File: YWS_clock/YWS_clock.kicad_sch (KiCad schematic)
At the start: 59 parts, among them J1 Conn_01x06, J2 PJ-102AH, J3 Conn_01x06, SW1 Omron_B3F_SPST, SW2 Omron_B3F_SPST, SW3 Omron_B3F_SPST, SW4 Omron_B3F_SPST, U1 L7805, U2 ATmega328-PU, U3 DS1307_DIP-8, U4 MAX7219, U5 MAX7219, U6 MAX7219, U7 MAX7219, Y1 Crystal_16MHz, Y2 Crystal_16MHz

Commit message: Add ICSP and separate sections
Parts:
- removed J2: PJ-102AH, footprints:PJ-102AH, symbol HPS:PJ-102AH
- removed R14: R_0805_10K, footprints:R_0805_2012Metric, symbol HPS:R_0805_10K
- removed R15: PhotoconductivePhotocell, footprints:R_LDR_4.9x4.2mm_P2.54mm_Vertical, symbol HPS:PhotoconductivePhotocell
- removed R5, R6: R_0805_2.2K, footprints:R_0805_2012Metric, symbol HPS:R_0805_2.2K
- added J2: Power_inlet_vertical, footprints:Wurth-694106402002, symbol HPS:Power_inlet_vertical
- added J4: Conn_01x06, footprints:PinHeader_2x03_P2.54mm_Vertical, symbol HPS:Conn_01x06
- added R14: PhotoconductivePhotocell, footprints:R_LDR_4.9x4.2mm_P2.54mm_Vertical, symbol HPS:PhotoconductivePhotocell
- added R15: R_0805_100K, footprints:R_0805_2012Metric, symbol HPS:R_0805_100K
- added R5, R6: R_0805_4.7K, footprints:R_0805_2012Metric, symbol HPS:R_0805_4.7K
- U1: footprint footprints:TO-220-3_Horizontal_TabDown -> footprints:TO-252-2
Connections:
- net GND: now also SW2.3 (B), SW2.4 (B), SW3.3 (B), SW3.4 (B), SW4.3 (B), SW4.4 (B), J2.2 (OUT), J4.6 (Pin_6), R15.2; no longer R11.2, R12.2, R13.2
- net LED_SCK: now also U2.19 (PB5), J4.3 (Pin_3); no longer U2.15 (PB1), U2.18 (PB4)
- net RESET: now also J4.5 (Pin_5)
- net RXD: now also U2.2 (PD0); no longer U2.12 (PD6)
- net TXD: now also U2.3 (PD1); no longer U2.13 (PD7)
- net VCC: now also R11.1, R12.1, R13.1, J4.2 (Pin_2), R14.1, R5.1, R6.1; no longer SW2.1 (A), SW2.2 (A), SW3.1 (A), SW3.2 (A), SW4.1 (A), SW4.2 (A)
- net at C6.1, U1.1 (IN): now also J2.1 (POLE)
- net BTN_SEL: now reaches U2.4 (PD2)
- net BTN_SEL: now also R11.2, SW2.1 (A), SW2.2 (A)
- net DISP_LOAD: now reaches U4.12 (LOAD), U5.12 (LOAD), U6.12 (LOAD), U7.12 (LOAD)
- net DISP_LOAD: now also U2.14 (PB0); no longer U2.16 (PB2)
- net DISP_CLK: now reaches U4.13 (CLK), U5.13 (CLK), U6.13 (CLK), U7.13 (CLK)
- net DISP_CLK: now also U2.15 (PB1); no longer U2.19 (PB5)
- net BTN_DOWN: now reaches U2.6 (PD4)
- net BTN_DOWN: now also R13.2, SW4.1 (A), SW4.2 (A)
- net SDA: now reaches U2.27 (PC4)
- net SDA: now also U3.5 (SDA), R6.2; no longer SW4.3 (B)
- net JOYST_X: now reaches J3.4 (Pin_4)
- net JOYST_X: now also U2.11 (PD5); no longer U2.23 (PC0)
- net BUZZER: now reaches U2.24 (PC1)
- net BUZZER: now also BZ1.2 (+); no longer J3.5 (Pin_5)
- net JOYST_Z: now reaches J3.6 (Pin_6)
- net JOYST_Z: now also U2.13 (PD7); no longer U2.11 (PD5)
- net SCL: now reaches U3.6 (SCL)
- net SCL: now also U2.28 (PC5), R5.2; no longer U2.2 (PD0)
- net DISP_DATA: now reaches U4.1 (DIN)
- net DISP_DATA: now also U2.16 (PB2); no longer U2.17 (PB3)
- net at U2.25 (PC2): no longer SW2.3 (B)
- net at U2.26 (PC3): no longer SW3.3 (B)
- net BTN_UP: now reaches U2.5 (PD3)
- net BTN_UP: now also R12.2, SW3.1 (A), SW3.2 (A); no longer BZ1.2 (+)
- new net JOYST_Y: J3.5 (Pin_5), U2.12 (PD6)
- new net LIGHT_SENSOR: R14.2, R15.1, U2.23 (PC0)
- new net MDSI: J4.4 (Pin_4)
- new net MISD: J4.1 (Pin_1)
- new net MISO: U2.18 (PB4)
- new net MOSI: U2.17 (PB3)
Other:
- note added: "Button"
- note added: "Buzzer"
- note added: "Dot Matrix with MAX7219"
- note added: "ICSP"
- note added: "JoyStick"
- note added: "Light Sensor"
- note added: "Mechanical"
- moved on the sheet: BT1, C1, C10, C11, C12, C13, C14, C15, C2, C3, C4, C5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

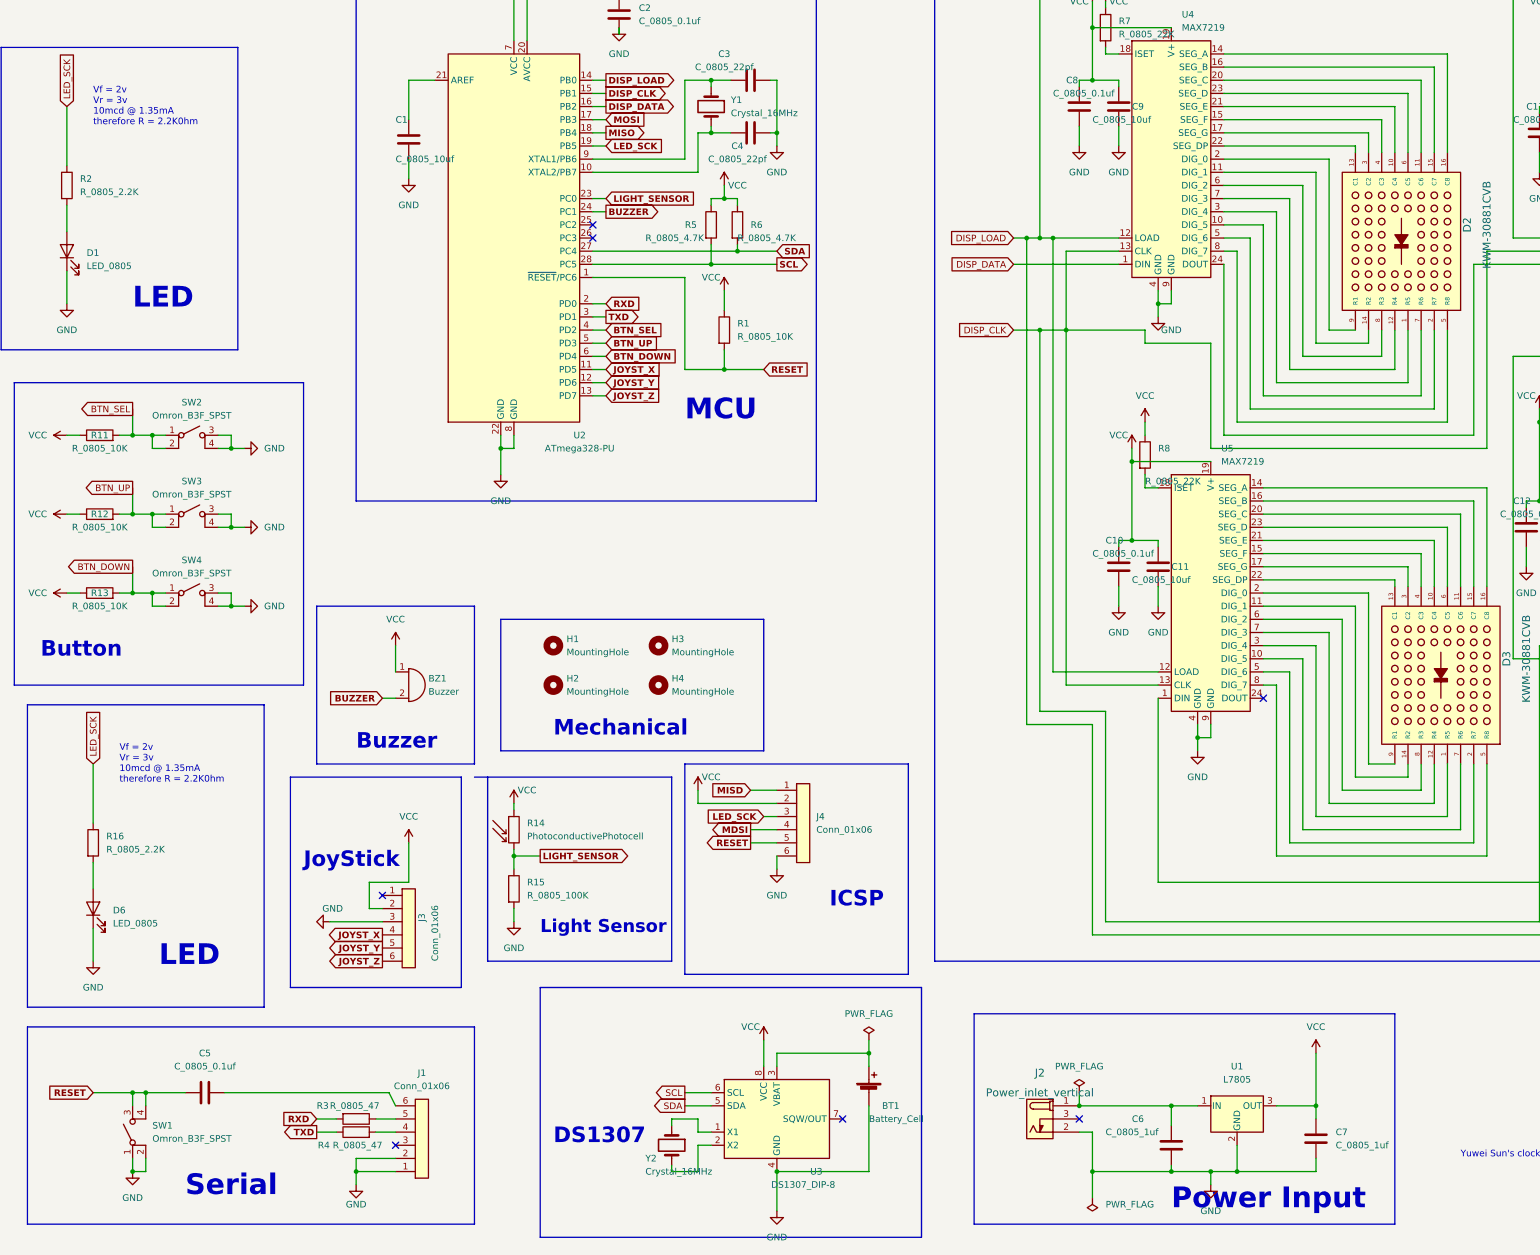
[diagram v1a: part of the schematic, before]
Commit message: Initial version with full routing and test point
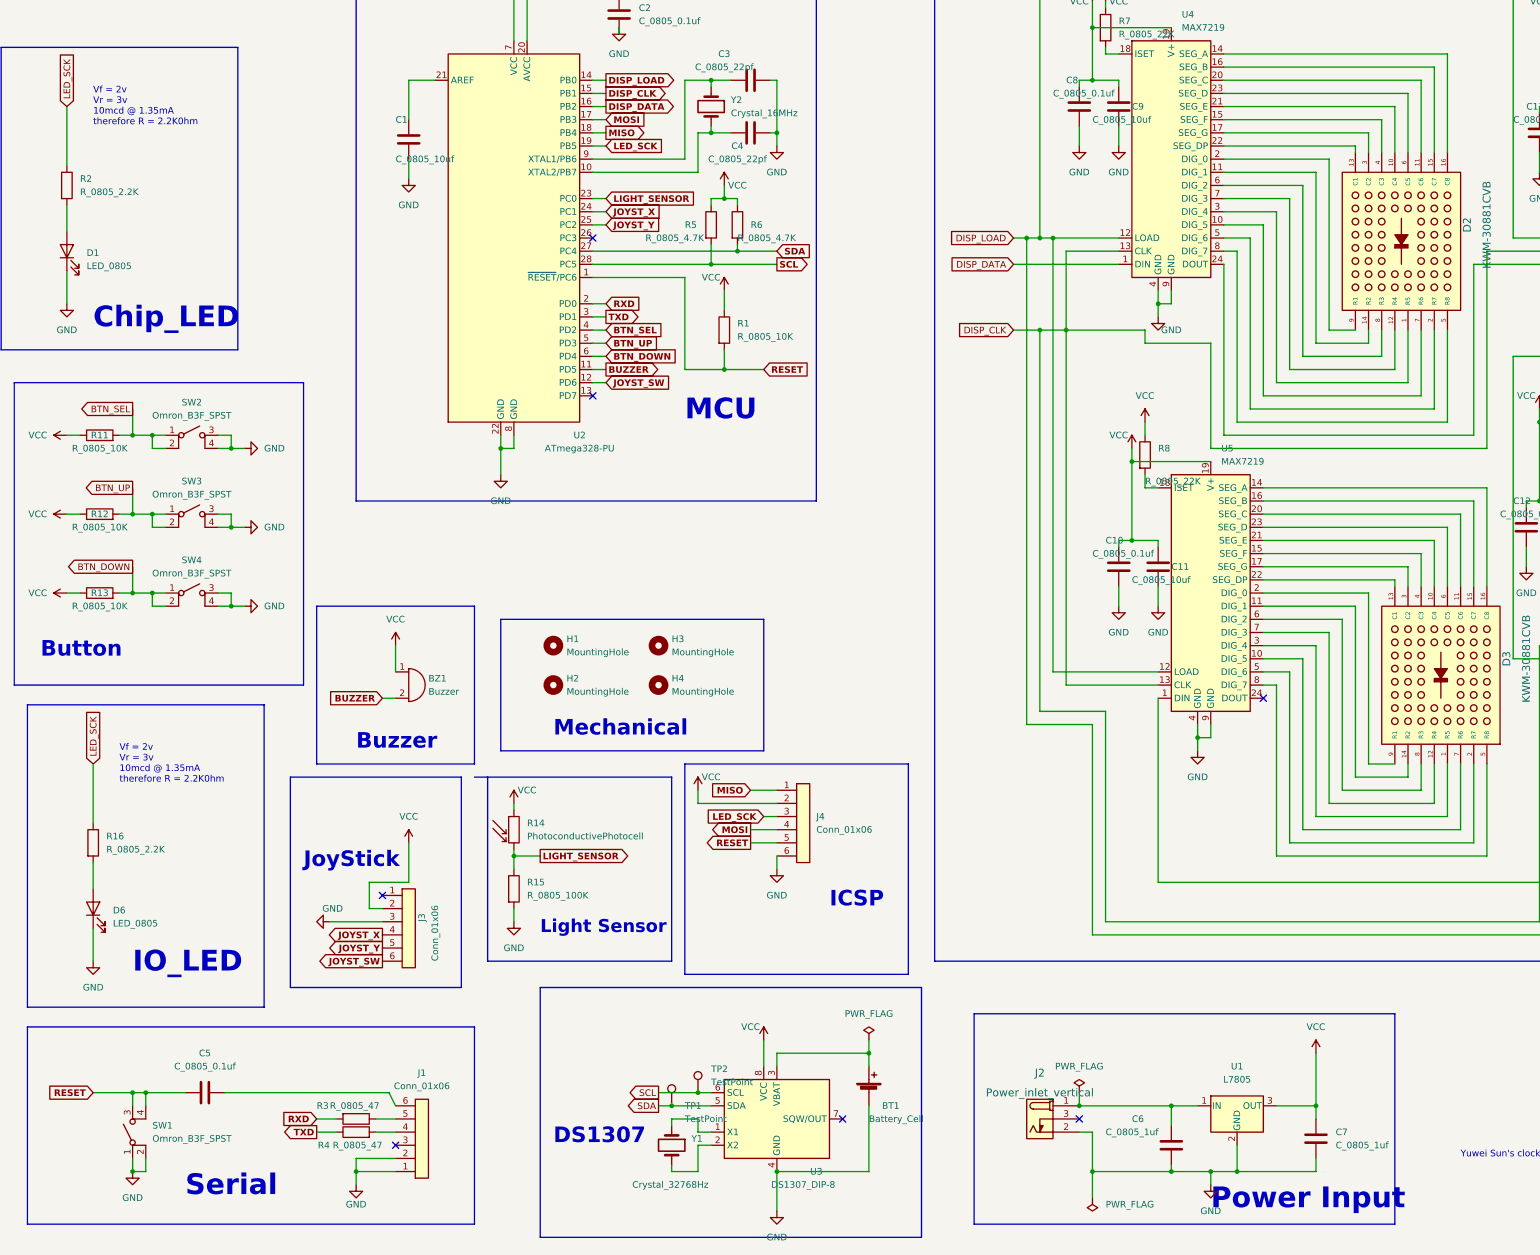
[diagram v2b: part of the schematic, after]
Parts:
- removed Y1: Crystal_16MHz, footprints:Crystal_SMD_HC49-SD, symbol HPS:Crystal_16MHz
- added TP1, TP2: TestPoint, footprints:TestPoint_THTPad_D2.0mm_Drill1.0mm, symbol HPS:TestPoint
- added Y1: Crystal_32768Hz, footprints:Crystal_SMD_2Pin_3.2x1.5mm, symbol HPS:Crystal_32768Hz
- U1: Digikey PN (none) -> 497-7255-1-ND; MFG (none) -> STMicroelectronics; MPN (none) -> L7805CDT-TR
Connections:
- net MDSI is gone; now on net MOSI: J4.4 (Pin_4)
- net MISD is gone; now on net MISO: J4.1 (Pin_1)
- net BUZZER: now also U2.11 (PD5); no longer U2.24 (PC1)
- net JOYST_X: now also U2.24 (PC1); no longer U2.11 (PD5)
- net JOYST_Y: now also U2.25 (PC2); no longer U2.12 (PD6)
- net SCL: now also TP2.1
- net SDA: now also TP1.1
- net at C3.1, U2.9 (XTAL1/PB6): now also Y2.1
- net at C4.1, U2.10 (XTAL2/PB7): now also Y2.2
- net at U3.1 (X1): now also Y1.1; no longer Y2.1
- net at U3.2 (X2): now also Y1.2; no longer Y2.2
- net JOYST_Z: no longer names the net of U2.13 (PD7)
- net JOYST_Z: no longer J3.6 (Pin_6)
- new net JOYST_SW: J3.6 (Pin_6), U2.12 (PD6)
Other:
- note added: "Chip_LED"
- note added: "IO_LED"
- note removed: "LED"
